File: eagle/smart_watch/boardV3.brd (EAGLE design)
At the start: 100 x 80 mm, 51 parts, among them U1 MCP73831, U2 TPS61200, U3 MAX1704X, U4 V_REG_LDOSMD, Y1 16MHz

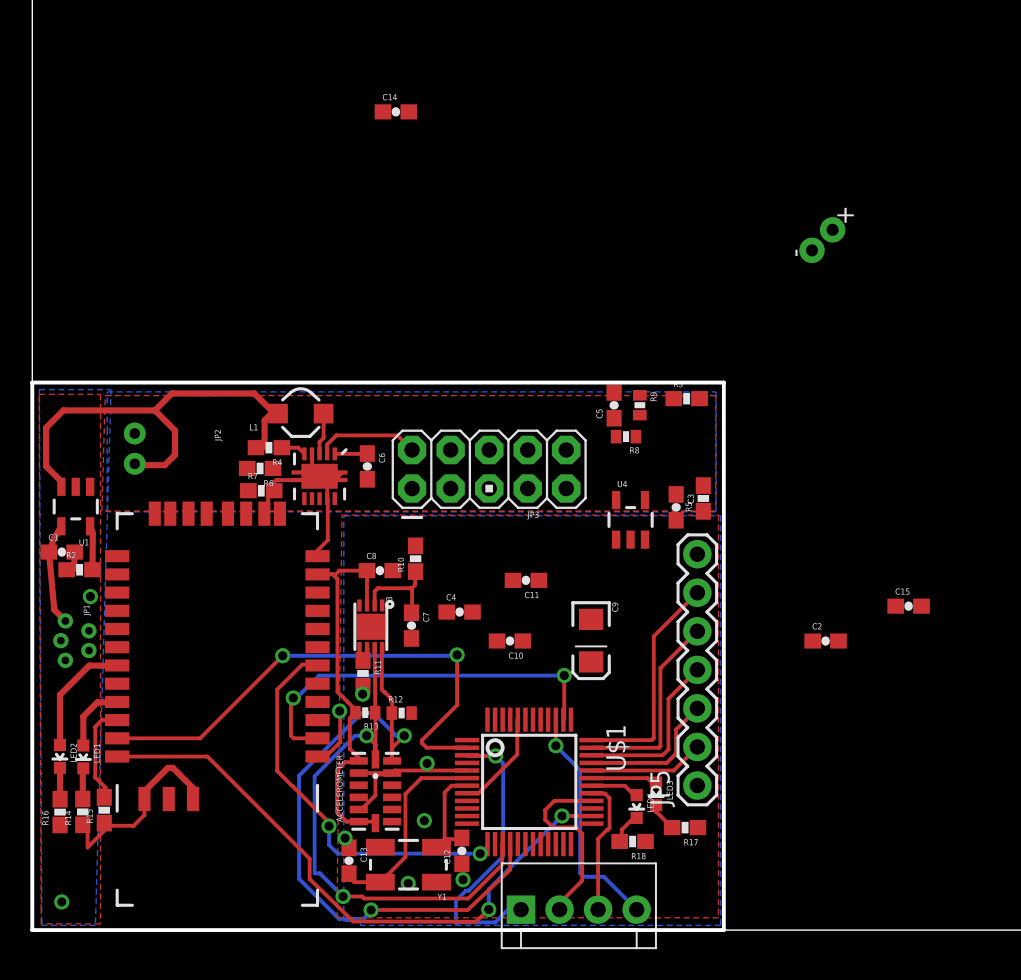
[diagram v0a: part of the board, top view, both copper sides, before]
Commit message: Finished off V3 board design. Added silk to boards
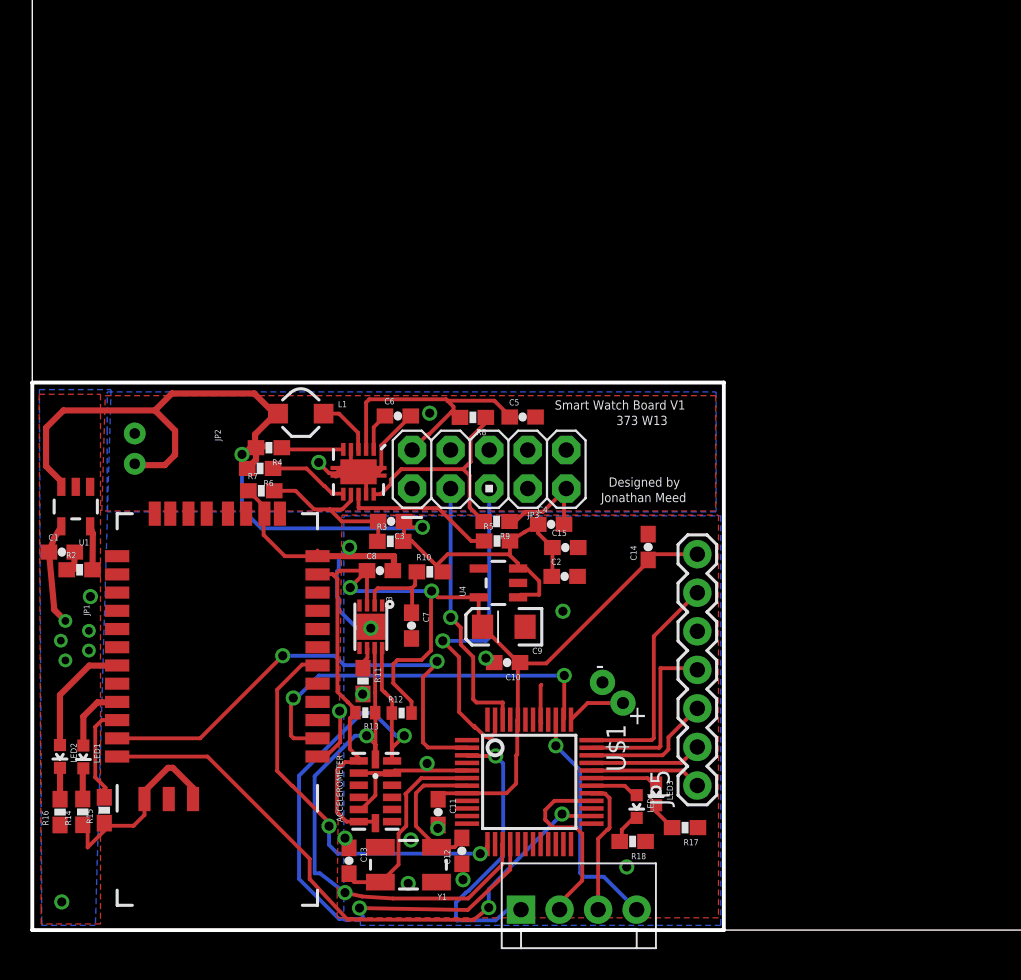
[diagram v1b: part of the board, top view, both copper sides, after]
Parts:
- R8, R9: device SparkFun-Passives:0402-RES -> SparkFun-Resistors:0603-RES
- moved C14 33.1 mm to (40.6, 25.2), turned to 90 degrees
- moved U$3 32.6 mm to (43.9, 18.9), turned to 0 degrees
- moved C15 22.9 mm to (35.1, 25.2)
- moved R3 21.7 mm to (23.6, 25.6)
- moved C3 18.8 mm to (23.6, 26.9), turned to 180 degrees
- moved C2 17.7 mm to (35.1, 23.3)
- moved C11 16.3 mm to (26.7, 7.77), turned to 270 degrees
- moved R5 13.9 mm to (30.6, 25.6), turned to 0 degrees
- moved R9 12.2 mm to (30.6, 26.9), turned to 180 degrees
- moved R8 10.2 mm to (29.0, 33.8)
- moved U4 9.65 mm to (30.7, 22.9), turned to 90 degrees
- moved C4 8.35 mm to (34.2, 26.7)
- moved C5 6.07 mm to (32.3, 33.8), turned to 0 degrees
- moved C9 5.82 mm to (31.1, 20.0), turned to 180 degrees
- moved C6 3.89 mm to (24.1, 33.9), turned to 0 degrees
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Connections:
- net GND: now also JP5.5; no longer JP5.1
- net JDOWN: now also JP5.2; no longer JP5.3
- net JLEFT: now also JP5.3; no longer JP5.4
- net JRIGHT: now also JP5.4; no longer JP5.5
- net JUP: now also JP5.1; no longer JP5.2
- net VIBE_PWM: now also U$1.37; no longer U$1.24
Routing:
- net 3.3V: track 33.0 -> 81.6 mm, vias 0 -> 2
- net VBATT: track 30.9 -> 74.0 mm, vias 0 -> 2
- net GND: track 45.2 -> 75.2 mm, vias 9 -> 17
- net SCTX: track 0.00 -> 22.4 mm, vias 0 -> 1
- net SCRX: track 0.00 -> 17.7 mm, vias 0 -> 1
- net N$8: track 0.00 -> 14.8 mm
- net 5V: track 6.86 -> 18.5 mm
- net N$3: track 0.00 -> 11.1 mm
- net N$6: track 0.00 -> 10.1 mm
- net N$5: track 0.00 -> 5.33 mm
- net VIBE_PWM: track 0.00 -> 3.88 mm
- net XTALOUT: track 6.65 -> 9.73 mm
- net JLEFT: track 11.3 -> 8.72 mm
- net VIN: track 1.66 -> 4.10 mm
- net SSEL1: track 34.5 -> 32.5 mm
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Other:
- board text added: "373 W13"
- board text added: "Designed by"
- board text added: "Jonathan Meed"
- board text added: "Smart Watch Board V1"

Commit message: Board and schema going out for review
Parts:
- added I2C: (no value), SparkFun-Connectors:1X02_PP_HOLES_ONLY
- added JP6: (no value), SparkFun-Connectors:1X07
- added LED5: (no value), SparkFun-LED:LED-0603
- added R1, R19, R20, R21, R22: 10k, SparkFun-Resistors:0603-RES
- added R23: 330, SparkFun-Passives:0603-RES
- added S1: (no value), SparkFun-Electromechanical:JOYSTICK_MINI
- added SPI: (no value), SparkFun-Connectors:MOLEX-1X4
- moved C14 7.55 mm to (36.2, 19.1), turned to 0 degrees
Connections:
- new net N$21: LED5.C, R23.2
- net 3.3V: now also JP6.7, LED5.A, R1.1, R19.1, R20.1, R21.1, R22.1
- net GND: now also JP6.5, R23.1, S1.GND
- net JCENTER: now also JP5.2, JP6.2, R22.2, S1.CTR, U$1.33; no longer JP5.6, U$1.36
- net JDOWN: now also JP5.4, JP6.4, R1.2, S1.D, U$1.35; no longer JP5.2, U$1.33
- net JLEFT: now also JP5.1, JP6.1, R20.2, S1.C, U$1.32; no longer JP5.3, U$1.34
- net JRIGHT: now also JP5.6, JP6.6, R21.2, S1.B, U$1.36; no longer JP5.4, U$1.35
- net JUP: now also JP5.3, JP6.3, R19.2, S1.A, U$1.34; no longer JP5.1, U$1.32
- net MISO1: now also SPI.2
- net MOSI1: now also SPI.1
- net SCK1: now also SPI.4
- net SCL: now also I2C.2
- net SDA: now also I2C.1
- net SSEL1: now also SPI.3
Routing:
- net 3.3V: track 81.6 -> 108.8 mm
- net JDOWN: track 7.41 -> 33.2 mm, vias 0 -> 1
- net JRIGHT: track 12.2 -> 35.5 mm
- net GND: track 75.2 -> 94.4 mm
- net MISO1: track 40.2 -> 57.5 mm, vias 2 -> 3
- net JUP: track 7.38 -> 23.7 mm
- net JLEFT: track 8.72 -> 23.3 mm
- net SCK1: track 26.1 -> 40.4 mm, vias 2 -> 4
- net MOSI1: track 25.8 -> 34.2 mm
- net JCENTER: track 14.9 -> 23.1 mm
- net SSEL1: track 32.5 -> 40.1 mm
- net SCL: track 35.2 -> 41.7 mm
- net N$21: track 0.00 -> 2.10 mm
- net SDA: track 44.6 -> 45.9 mm
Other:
- board size 100 x 80 mm -> 160 x 181.6 mm
- board text added: "David Jackson"
- board text added: "EECS 373 W2013"
- board text added: "Joystick V1"

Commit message: Out for review
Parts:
- moved R11 0.18 mm to (21.7, 16.5)
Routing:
- net GND: track 94.4 -> 110.6 mm
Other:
- board size 160 x 181.6 mm -> 100 x 80.3 mm
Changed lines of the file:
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@@
 <layers>
 <layer number="1" name="Top" color="4" fill="1" visible="yes" active="yes"/>
-<layer number="2" name="Route2" color="1" fill="3" visible="no" active="yes"/>
-<layer number="3" name="Route3" color="4" fill="3" visible="no" active="yes"/>
-<layer number="4" name="Route4" color="1" fill="4" visible="no" active="yes"/>
-<layer number="5" name="Route5" color="4" fill="4" visible="no" active="yes"/>
-<layer number="6" name="Route6" color="1" fill="8" visible="no" active="yes"/>
-<layer number="7" name="Route7" color="4" fill="8" visible="no" active="yes"/>
-<layer number="8" name="Route8" color="1" fill="2" visible="no" active="yes"/>
-<layer number="9" name="Route9" color="4" fill="2" visible="no" active="yes"/>
-<layer number="10" name="Route10" color="1" fill="7" visible="no" active="yes"/>
-<layer number="11" name="Route11" color="4" fill="7" visible="no" active="yes"/>
-<layer number="12" name="Route12" color="1" fill="5" visible="no" active="yes"/>
-<layer number="13" name="Route13" color="4" fill="5" visible="no" active="yes"/>
-<layer number="14" name="Route14" color="1" fill="6" visible="no" active="yes"/>
-<layer number="15" name="Route15" color="4" fill="6" visible="no" active="yes"/>
+<layer number="2" name="Route2" color="1" fill="3" visible="yes" active="yes"/>
+<layer number="3" name="Route3" color="4" fill="3" visible="yes" active="yes"/>
+<layer number="4" name="Route4" color="1" fill="4" visible="yes" active="yes"/>
+<layer number="5" name="Route5" color="4" fill="4" visible="yes" active="yes"/>
+<layer number="6" name="Route6" color="1" fill="8" visible="yes" active="yes"/>
+<layer number="7" name="Route7" color="4" fill="8" visible="yes" active="yes"/>
+<layer number="8" name="Route8" color="1" fill="2" visible="yes" active="yes"/>
+<layer number="9" name="Route9" color="4" fill="2" visible="yes" active="yes"/>
+<layer number="10" name="Route10" color="1" fill="7" visible="yes" active="yes"/>
+<layer number="11" name="Route11" color="4" fill="7" visible="yes" active="yes"/>
+<layer number="12" name="Route12" color="1" fill="5" visible="yes" active="yes"/>
+<layer number="13" name="Route13" color="4" fill="5" visible="yes" active="yes"/>
+<layer number="14" name="Route14" color="1" fill="6" visible="yes" active="yes"/>
+<layer number="15" name="Route15" color="4" fill="6" visible="yes" active="yes"/>
 <layer number="16" name="Bottom" color="1" fill="1" visible="yes" active="yes"/>
 <layer number="17" name="Pads" color="2" fill="1" visible="yes" active="yes"/>
@@
 <layer number="49" name="Reference" color="7" fill="1" visible="no" active="yes"/>
 <layer number="50" name="dxf" color="7" fill="1" visible="no" active="no"/>
-<layer number="51" name="tDocu" color="6" fill="1" visible="no" active="yes"/>
+<layer number="51" name="tDocu" color="6" fill="1" visible="yes" active="yes"/>
 <layer number="52" name="bDocu" color="7" fill="1" visible="no" active="yes"/>
 <layer number="53" name="tGND_GNDA" color="7" fill="9" visible="no" active="no"/>
@@
 <text x="37.973" y="29.21" size="0.6096" layer="25" font="vector">Designed by</text>
 <text x="37.465" y="28.194" size="0.6096" layer="25" font="vector">Jonathan Meed</text>
-<wire x1="160" y1="-101.6" x2="160" y2="-1.6" width="0" layer="20"/>
 <wire x1="46.482" y1="8.128" x2="46.482" y2="25.908" width="0.4064" layer="20"/>
 <wire x1="46.482" y1="25.908" x2="62.992" y2="25.908" width="0.4064" layer="20"/>
@@
 <attribute name="VALUE" x="26.95306875" y="24.362671875" size="0.4064" layer="27" font="vector"/>
 </element>
-<element name="R11" library="SparkFun-Passives" package="0603-RES" value="4.7k" x="21.787621875" y="16.403865625" smashed="yes" rot="R270">
-<attribute name="NAME" x="22.549621875" y="17.292865625" size="0.4064" layer="25" font="vector" rot="R270"/>
-<attribute name="VALUE" x="20.644621875" y="17.038865625" size="0.4064" layer="27" font="vector" rot="R270"/>
+<element name="R11" library="SparkFun-Passives" package="0603-RES" value="4.7k" x="21.660621875" y="16.530865625" smashed="yes" rot="R270">
+<attribute name="NAME" x="22.422621875" y="17.419865625" size="0.4064" layer="25" font="vector" rot="R270"/>
+<attribute name="VALUE" x="20.517621875" y="17.165865625" size="0.4064" layer="27" font="vector" rot="R270"/>
 </element>
 <element name="C7" library="SparkFun-Passives" package="0603-CAP" value="1uF" x="24.982959375" y="20.061203125" smashed="yes" rot="R270">
@@
 <wire x1="43.815" y1="19.685" x2="51.435" y2="19.685" width="0.4064" layer="16"/>
 <contactref element="R23" pad="1"/>
+<wire x1="21.76451875" y1="15.544278125" x2="24.892" y2="15.544278125" width="0.4064" layer="16"/>
+<wire x1="24.892" y1="15.544278125" x2="24.892" y2="9.017" width="0.4064" layer="16"/>
+<wire x1="21.660621875" y1="15.680865625" x2="21.276134375" y2="15.680865625" width="0.4064" layer="1"/>
+<wire x1="21.276134375" y1="15.680865625" x2="20.574" y2="16.383" width="0.4064" layer="1"/>
+<wire x1="20.574" y1="16.383" x2="20.574" y2="19.558" width="0.4064" layer="1"/>
+<wire x1="20.574" y1="19.558" x2="21.1455" y2="20.1295" width="0.4064" layer="1"/>
+<wire x1="21.1455" y1="20.1295" x2="22.160646875" y2="20.1295" width="0.4064" layer="1"/>
+<wire x1="22.160646875" y1="20.1295" x2="22.305275" y2="19.984871875" width="0.4064" layer="1"/>
 </signal>
 <signal name="N$2">
@@
 <contactref element="U3" pad="6"/>
 <contactref element="R11" pad="1"/>
-<wire x1="21.787621875" y1="17.253865625" x2="21.787621875" y2="17.648696875" width="0.254" layer="1"/>
+<wire x1="21.660621875" y1="17.380865625" x2="21.787621875" y2="17.648696875" width="0.254" layer="1"/>
 <wire x1="21.787621875" y1="17.648696875" x2="22.080709375" y2="17.941784375" width="0.254" layer="1"/>
 <wire x1="22.080709375" y1="17.941784375" x2="22.080709375" y2="18.5594375" width="0.254" layer="1"/>
@@
 <wire x1="18.602603125" y1="10.1433" x2="18.602603125" y2="3.74140625" width="0.254" layer="16"/>
 <wire x1="30.986771875" y1="5.66028125" x2="30.990290625" y2="5.6638" width="0.254" layer="1"/>
-<via x="20.600403125" y="2.467084375" extent="1-16" drill="0.6"/>
+<via x="20.219403125" y="2.340084375" extent="1-16" drill="0.6"/>
 <wire x1="18.602603125" y1="3.74140625" x2="18.94508125" y2="3.74140625" width="0.254" layer="16"/>
-<wire x1="18.94508125" y1="3.74140625" x2="20.600403125" y2="2.467084375" width="0.254" layer="16"/>
-<wire x1="20.600403125" y1="2.467084375" x2="21.738184375" y2="2.213084375" width="0.254" layer="1"/>
-<wire x1="21.738184375" y1="2.213084375" x2="23.774915625" y2="2.081353125" width="0.254" layer="1"/>
+<wire x1="18.94508125" y1="3.74140625" x2="20.219403125" y2="2.340084375" width="0.254" layer="16"/>
+<wire x1="20.219403125" y1="2.340084375" x2="21.230184375" y2="2.340084375" width="0.254" layer="1"/>
+<wire x1="21.230184375" y1="2.340084375" x2="23.774915625" y2="2.081353125" width="0.254" layer="1"/>
 <wire x1="23.774915625" y1="2.081353125" x2="28.72099375" y2="2.081353125" width="0.254" layer="1"/>
 <wire x1="28.72099375" y1="2.081353125" x2="30.960421875" y2="4.32078125" width="0.254" layer="1"/>
@@
 <wire x1="15.113" y1="2.032" x2="16.51" y2="3.429" width="0.254" layer="1"/>
 <wire x1="16.51" y1="3.429" x2="19.6384875" y2="3.429" width="0.254" layer="1"/>
-<wire x1="19.6384875" y1="3.429" x2="20.600403125" y2="2.467084375" width="0.254" layer="1"/>
+<wire x1="19.6384875" y1="3.429" x2="20.219403125" y2="2.340084375" width="0.254" layer="1"/>
 </signal>
 <signal name="SDA">
@@
 <contactref element="U$1" pad="26"/>
 <contactref element="U$2" pad="24"/>
-<wire x1="20.764503125" y1="0.69413125" x2="21.20856875" y2="0.69315625" width="0.254" layer="1"/>
-<wire x1="21.20856875" y1="0.69315625" x2="29.085128125" y2="0.6758375" width="0.254" layer="1"/>
+<wire x1="20.764503125" y1="0.69413125" x2="20.70056875" y2="0.69315625" width="0.254" layer="1"/>
+<wire x1="20.70056875" y1="0.69315625" x2="29.085128125" y2="0.6758375" width="0.254" layer="1"/>
 <wire x1="29.085128125" y1="0.6758375" x2="30.071978125" y2="1.4808" width="0.254" layer="1"/>
 <via x="30.071978125" y="1.4808" extent="1-16" drill="0.6"/>
@@
 <wire x1="13.843" y1="0.889" x2="14.097" y2="0.635" width="0.254" layer="1"/>
 <wire x1="14.097" y1="0.635" x2="21.1504125" y2="0.635" width="0.254" layer="1"/>
-<wire x1="21.1504125" y1="0.635" x2="21.20856875" y2="0.69315625" width="0.254" layer="1"/>
+<wire x1="21.1504125" y1="0.635" x2="20.70056875" y2="0.69315625" width="0.254" layer="1"/>
 <wire x1="9.648" y1="11.434" x2="7.489" y2="11.434" width="0.254" layer="1"/>
 <wire x1="7.489" y1="11.434" x2="7.366" y2="11.557" width="0.254" layer="1"/>
@@
 </signal>
 </signals>
+<errors>
+</errors>
 </board>
 </drawing>
